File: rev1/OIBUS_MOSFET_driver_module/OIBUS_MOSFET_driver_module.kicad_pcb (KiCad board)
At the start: 2 copper layers, 90.2 x 95.9 mm, 139 parts, among them J1 SWD, J10 +, J11 +, J12 +, J13 +, J2 UART, J3 5V - 24V, Molex Ultrafit, J4 +, J5 +, J6 +, J7 +, J8 +, J9 +, T1 DMG6402LVT, T10 DMG6402LVT, T2 DMG6402LVT, T3 DMG6402LVT, T4 DMG6402LVT, T5 DMG6402LVT, T6 DMG6402LVT, T7 DMG6402LVT, T8 DMG6402LVT, T9 DMG6402LVT, U1 TLP291, U10 STM32F303CCTx, U11 TLP291, U12 TLP291, U2 TLP291, U3 TLP291, U4 TLP291, U5 TLP291, U6 TLP291, U7 TLP291, U8 TLP291, U9 TCAN330, Y1 16M

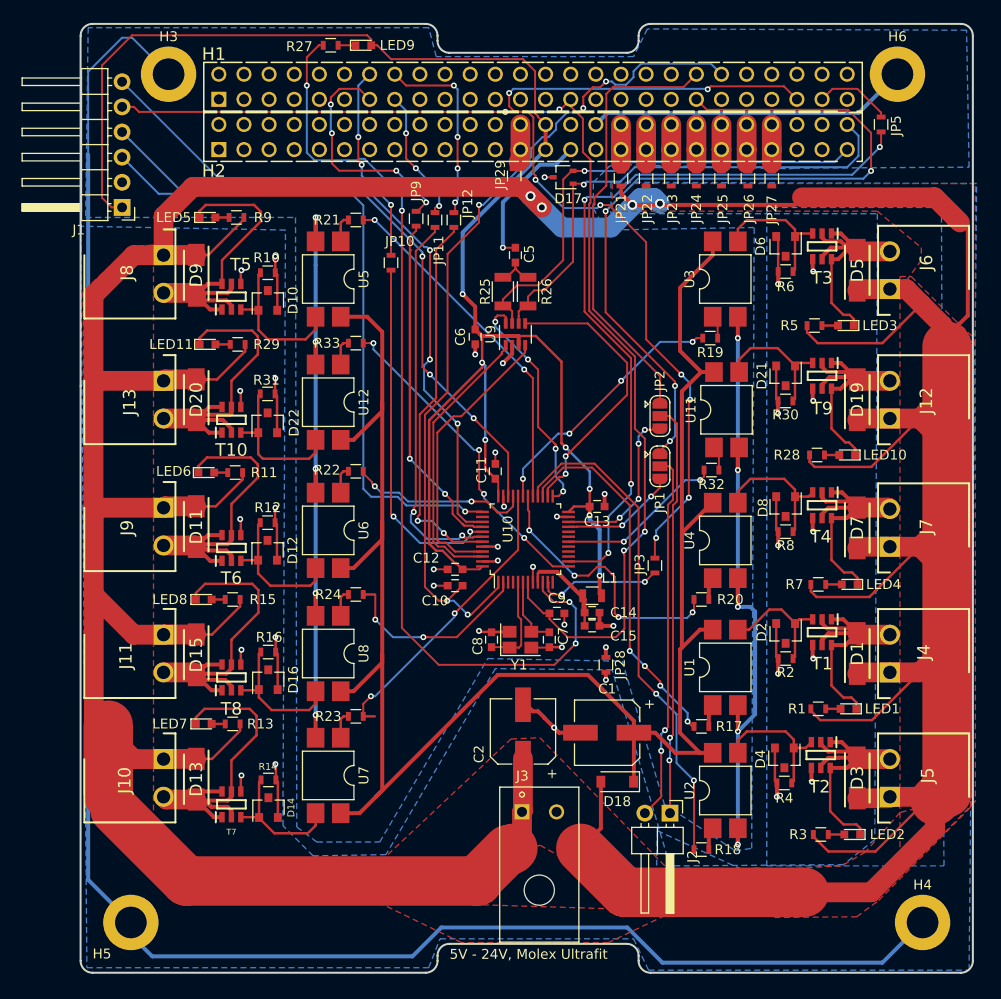
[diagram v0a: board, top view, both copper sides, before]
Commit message: removing vbus loop adding more 0ohms for connecting DGND to GND
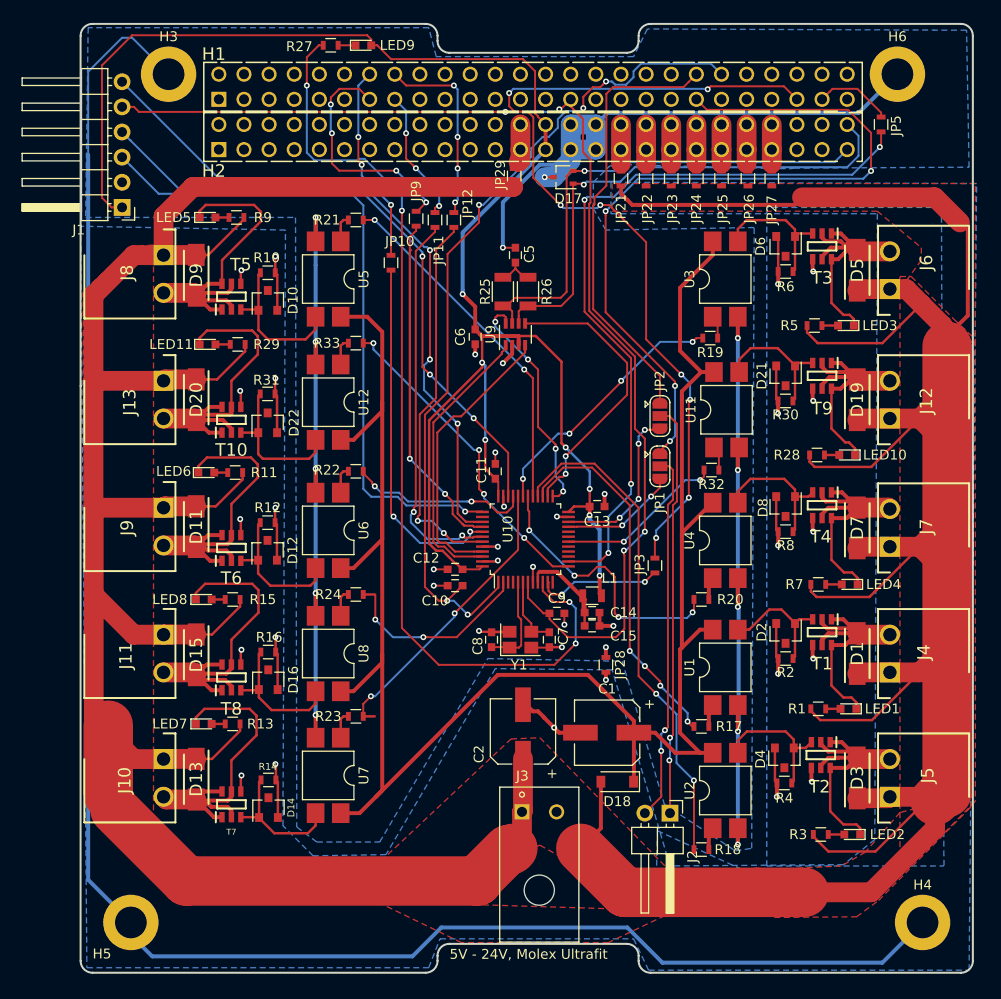
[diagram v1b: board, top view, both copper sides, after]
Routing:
- net VBUS: track 566.1 -> 546.3 mm, vias 4 -> 0
- net GND: track 385.8 -> 398.3 mm
- net CANL: track 51.0 -> 52.3 mm
- net CANH: track 48.9 -> 50.2 mm

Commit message: adding more jumpers, removing newer kicad footprint paths from project into global, adding fiducials
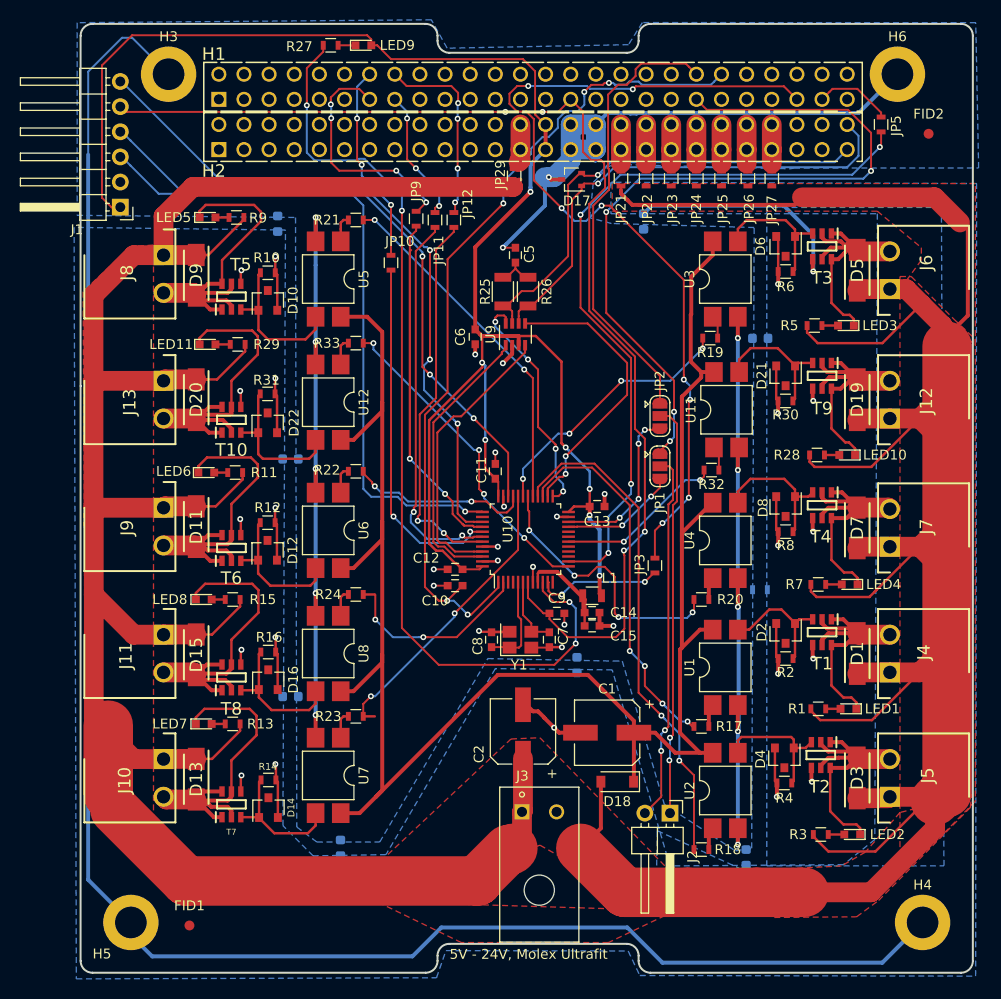
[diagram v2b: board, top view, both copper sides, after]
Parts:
- added FID1: Fiducial, Fiducial:Fiducial_1mm_Dia_2mm_Outer, F.Cu at (59.4, 134.2)
- added FID2: Fiducial, Fiducial:Fiducial_1mm_Dia_2mm_Outer, F.Cu at (134.1, 54.2)
- added JP13: 0 OHM, Resistor_SMD:R_0603_1608Metric, B.Cu at (74.7, 126.3)
- added JP14: 0 OHM, Resistor_SMD:R_0603_1608Metric, B.Cu at (117.1, 74.8)
- added JP15: 0 OHM, Resistor_SMD:R_0603_1608Metric, B.Cu at (68.3, 63.2)
- added JP16: 0 OHM, Resistor_SMD:R_0603_1608Metric, B.Cu at (98.6, 107.8)
- added JP4: 0 OHM, Resistor_SMD:R_0603_1608Metric, B.Cu at (115.6, 127.3)
- added JP6: 0 OHM, Resistor_SMD:R_0603_1608Metric, B.Cu at (105.3, 63.0)
- added JP7: 0 OHM, Resistor_SMD:R_0603_1608Metric, B.Cu at (69.6, 87.0)
- added JP8: 0 OHM, Resistor_SMD:R_0603_1608Metric, B.Cu at (69.6, 111.0)
- JP28: moved to B.Cu
- moved JP28 17.3 mm to (117.0, 100.2), turned to 0 degrees
- moved D17 0.89 mm to (98.0, 58.8)
- moved J1 0.18 mm to (52.4, 61.6)
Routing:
- net GNDPWR: track 74.8 -> 96.4 mm, vias 22 -> 21
- net CANH: track 50.2 -> 47.5 mm
- net CANL: track 52.3 -> 49.9 mm
- net ~RESET: track 117.5 -> 119.3 mm
- net VBACKUP: track 86.4 -> 85.2 mm
- net Net-(H1-Pad40): track 44.5 -> 45.7 mm
- net Net-(H1-Pad47): track 89.9 -> 91.0 mm
- net +3V3: track 176.1 -> 175.1 mm
- net Vopto: track 190.6 -> 189.7 mm
- net In3: track 26.5 -> 27.1 mm
- net GND: track 398.3 -> 398.1 mm, vias 28 -> 27

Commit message: adding finishing touches
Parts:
- added G***: LOGO, lib_fp_global:octanis_instruments_logo, F.Cu at (70.6, 129.7)
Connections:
- JP1 pad 2: Net-(J2-Pad2) -> Tx
- JP1 pad 3: Tx -> Net-(J2-Pad2)
- JP2 pad 2: Net-(J2-Pad1) -> Rx
- JP2 pad 3: Rx -> Net-(J2-Pad1)
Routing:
- net GND: track 398.1 -> 395.1 mm
- net Net-(J2-Pad2): track 37.3 -> 35.1 mm
- net Tx: track 11.7 -> 13.7 mm
- net Net-(J2-Pad1): track 41.7 -> 40.5 mm
- net In7: track 30.2 -> 29.0 mm
- net Rx: track 16.9 -> 17.9 mm
- net Net-(H1-Pad13): track 24.1 -> 23.2 mm
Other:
- board text added: "1"
- board text added: "3V3"
- board text added: "5..24 V"
- board text added: "GND"
- board text added: "OIBUS"
- board text added: "OIBUS 104.1 (P4L4)(V*)(USER02)(COMM)"
- board text added: "OIBUS MOSFET driver Revision 1, 2018, SS Octanis Instruments OÜ www.octanis.ch"
- board text added: "RX"
- board text added: "SWDCLK"
- board text added: "SWDIO"
- board text added: "SWO"
- board text added: "TX"
- board text added: "~RESET"
- board text removed: "OIBUS MOSFET driver Revision 1, 2018, SS Octanis Instruments OÜ"

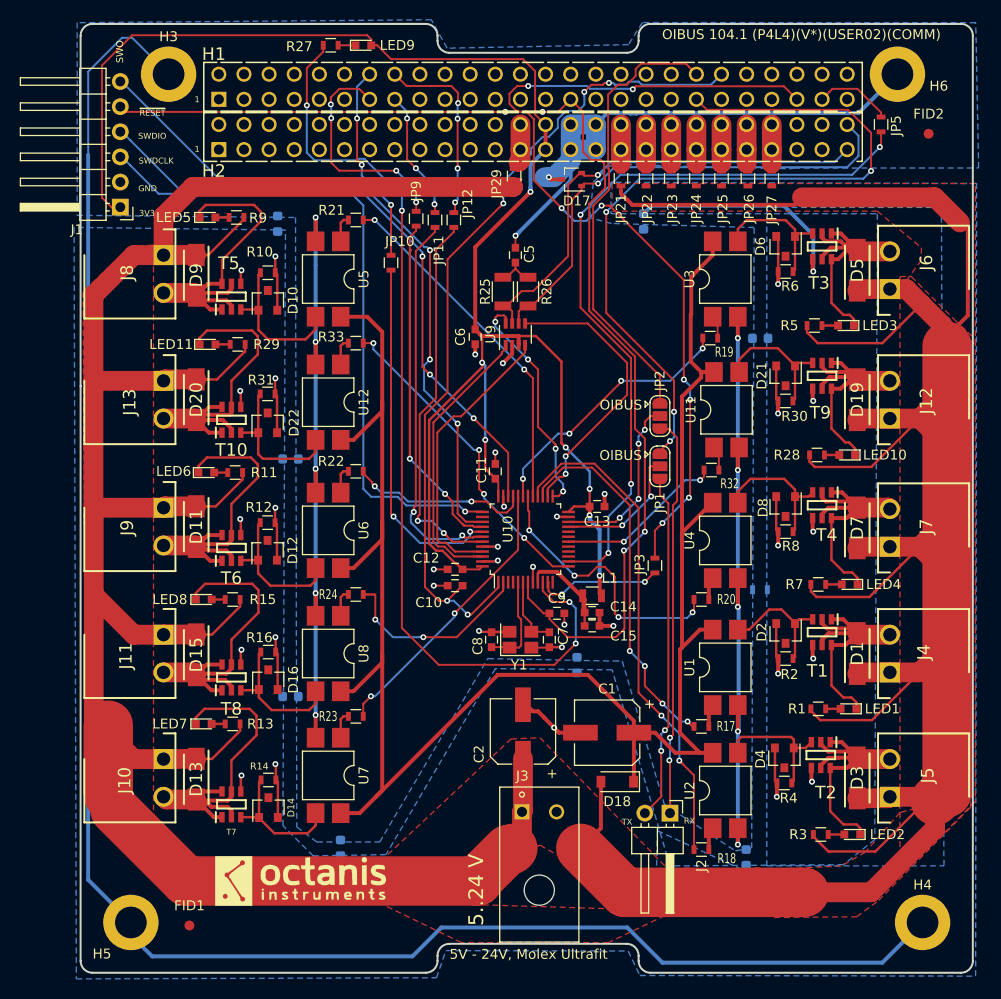
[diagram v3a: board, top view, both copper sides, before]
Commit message: fixed wrong optocoupler footprint
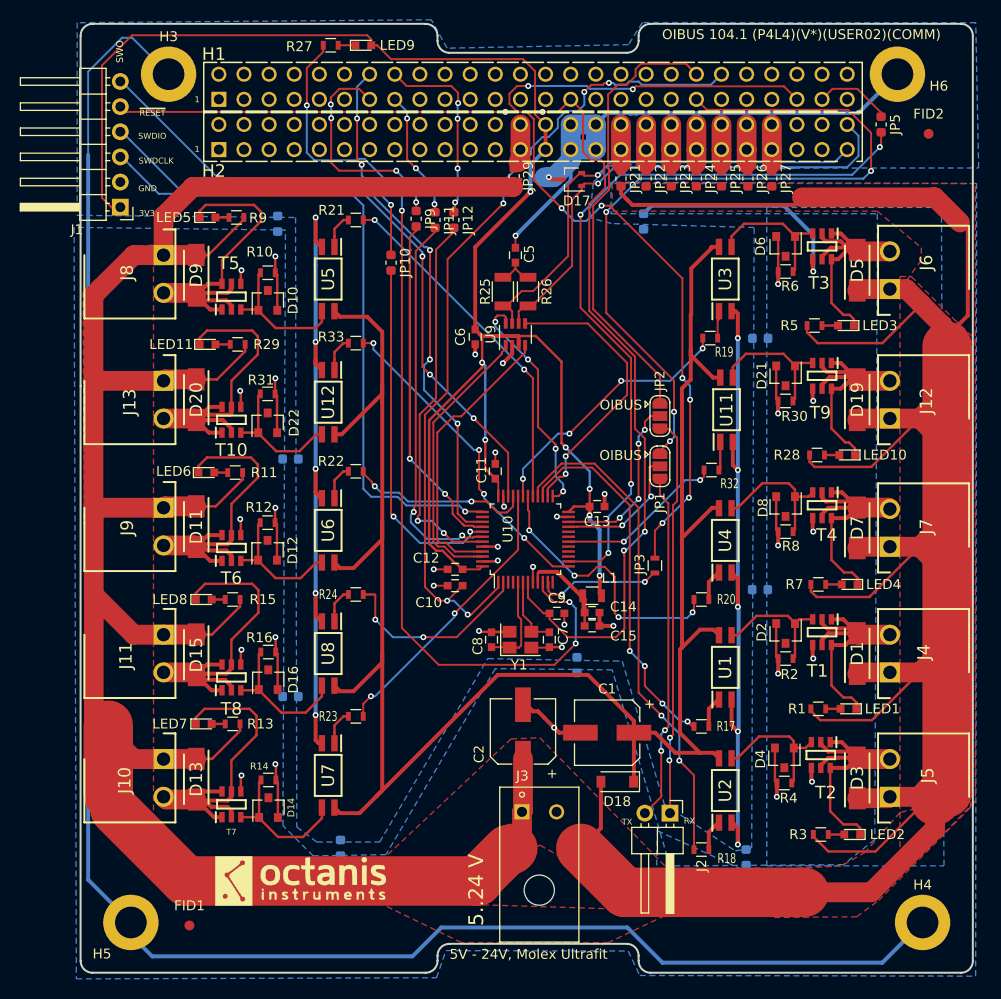
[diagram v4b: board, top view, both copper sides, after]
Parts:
- JP10, JP11, JP12, JP21, JP22, JP23, JP24, JP25, JP26, JP27, JP28, JP29, JP5, JP9: footprint Resistors_SMD:R_0603 -> Resistor_SMD:R_0603_1608Metric
- U1, U11, U12, U2, U3, U4, U5, U6, U7, U8: footprint Package_DIP:SMDIP-4_W7.62mm -> TLP291(SE:SOIC127P700X220-4N
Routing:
- net Vopto: track 189.7 -> 199.1 mm
- net GND: track 395.1 -> 404.3 mm
- net GateT10: track 15.4 -> 13.7 mm
- net GateT5: track 15.5 -> 14.2 mm
- net GateT6: track 14.8 -> 13.5 mm
- net GateT7: track 13.7 -> 14.8 mm
- net Net-(R20-Pad1): track 2.32 -> 3.19 mm
- net Net-(R18-Pad1): track 2.32 -> 3.19 mm
- net Net-(R17-Pad1): track 2.32 -> 3.19 mm
- net Net-(R23-Pad1): track 2.77 -> 3.60 mm
- net Net-(R21-Pad1): track 2.77 -> 3.60 mm
- net Net-(R33-Pad1): track 2.77 -> 3.60 mm
- net Net-(R24-Pad1): track 2.77 -> 3.60 mm
- net Net-(R22-Pad1): track 2.77 -> 3.60 mm
- net GateT8: track 14.3 -> 14.8 mm
